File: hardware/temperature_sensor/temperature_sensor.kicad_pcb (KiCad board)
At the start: 2 copper layers, 22 x 36 mm, 26 parts, among them J1 Conn_01x02_Male, J2 USB_C_Receptacle_USB2.0_16P, J3 Conn_01x04_Socket, U1 ESP32-C6-MINI-1/U, U2 BME280, U3 MCP1700x-330xxTT, U4 TPD4E02B04DQA

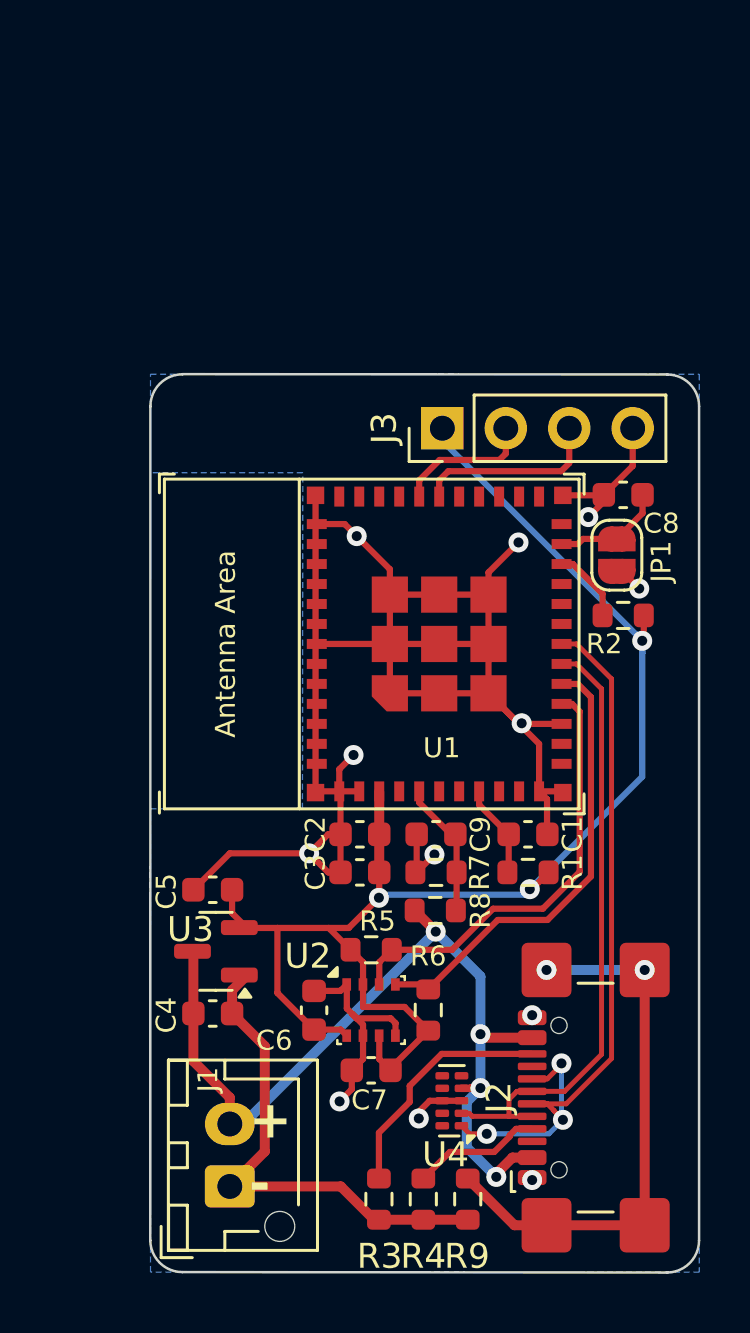
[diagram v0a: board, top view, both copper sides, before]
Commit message: Update schema and PCB, more caps, antenna hanging free
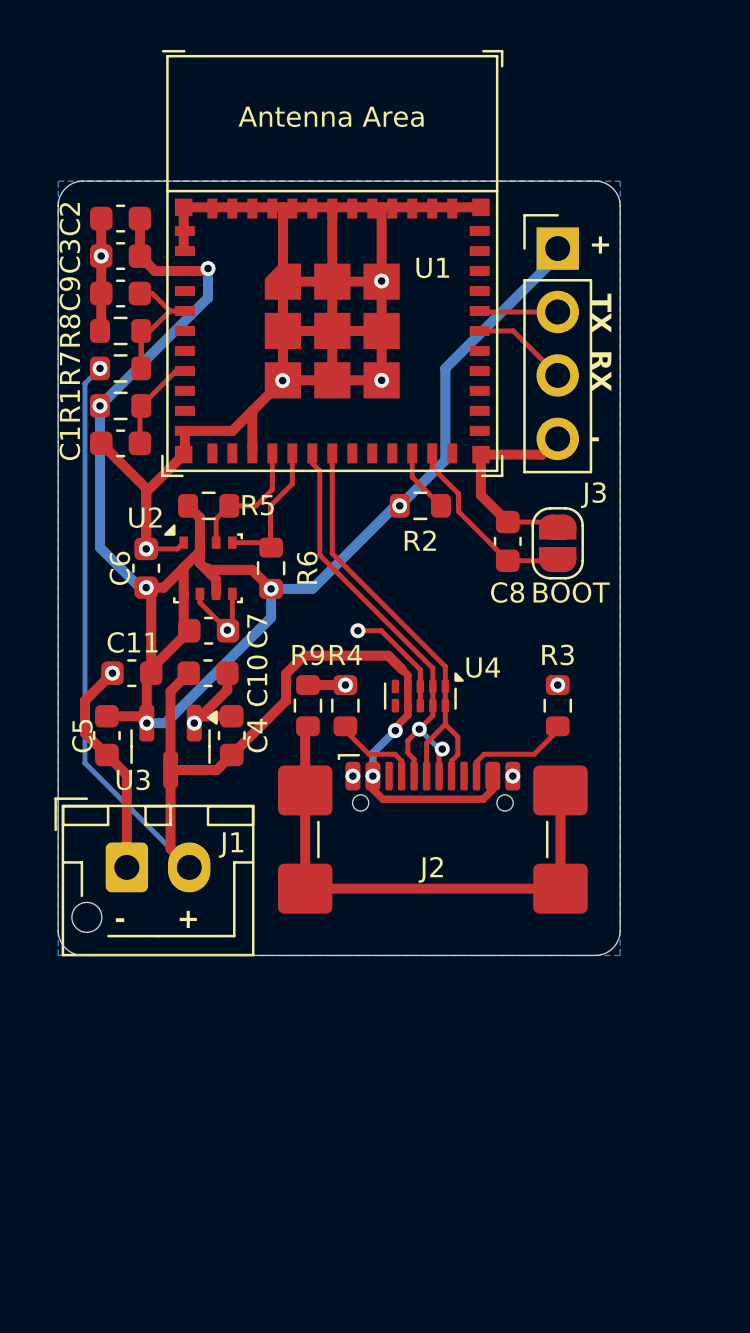
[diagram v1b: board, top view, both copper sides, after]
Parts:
- removed JP1: SolderJumper_2_Open, Jumper:SolderJumper-2_P1.3mm_Open_RoundedPad1.0x1.5mm
- added BOOT: SolderJumper_2_Open, Jumper:SolderJumper-2_P1.3mm_Open_RoundedPad1.0x1.5mm, F.Cu at (117.5, 55.7)
- added C10: 47µF, Capacitor_SMD:C_0603_1608Metric, F.Cu at (103.5, 60.9)
- added C11: 47µF, Capacitor_SMD:C_0603_1608Metric, F.Cu at (100.5, 60.9)
- C1: value 1µF/16V -> 1µF
- C2: value 0.1µF/50V -> 100nF
- C3: value 10µF/20V -> 10µF
- C8: value 0.1µF -> 100nF
- moved C3 26.5 mm to (100.0, 44.2)
- moved C2 26.4 mm to (100.0, 42.7)
- moved R7 25.1 mm to (100.0, 48.7)
- moved R8 25.1 mm to (100.0, 47.2)
- moved C9 25.1 mm to (100.0, 45.7)
- moved R1 24.8 mm to (100.0, 50.2), turned to 0 degrees
- moved C1 22.6 mm to (100.0, 51.7), turned to 0 degrees
- moved R3 21.0 mm to (117.5, 62.2), turned to 90 degrees
- moved R9 20.8 mm to (107.5, 62.2), turned to 90 degrees
- moved R4 20.0 mm to (109.0, 62.2), turned to 90 degrees
- moved C6 18.9 mm to (101.0, 56.7)
- moved R5 18.9 mm to (103.5, 54.2)
- moved U2 18.9 mm to (103.5, 56.7)
- moved R6 18.8 mm to (106.0, 56.7)
- moved C7 18.8 mm to (103.5, 59.2), turned to 0 degrees
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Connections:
- U4 pad 10: unconnected-(U4-NC-Pad10) -> /USB_D+
- U4 pad 7: unconnected-(U4-NC-Pad7) -> +BATT
- U4 pad 9: unconnected-(U4-NC-Pad9) -> /USB_D-
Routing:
- net +BATT: track 35.9 -> 53.5 mm, vias 4 -> 3
- net /USB_D+: track 31.4 -> 17.5 mm, vias 3 -> 0
- net /I2C_SCL: track 18.4 -> 5.78 mm
- net /I2C_SDA: track 17.7 -> 5.14 mm
- net GND: track 108.9 -> 100.4 mm, vias 12 -> 13
- net /USB_D-: track 24.7 -> 17.8 mm, vias 0 -> 2
- net +3.3V: track 64.1 -> 69.5 mm, vias 3 -> 6
- net Net-(J2-CC2): track 9.65 -> 4.51 mm
- net /U0RXD: track 7.54 -> 3.86 mm
- net /BOOT_MODE: track 4.49 -> 7.57 mm
- net /U0TXD: track 5.58 -> 3.14 mm
- net Net-(J2-CC1): track 5.21 -> 3.53 mm
- net Net-(J2-SHIELD): track 22.0 -> 20.7 mm, vias 2 -> 0
- net /ADC: track 5.40 -> 6.37 mm
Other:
- board size 22 x 36 mm -> 22.5 x 31 mm
- board text added: "RX"
- board text added: "TX"
